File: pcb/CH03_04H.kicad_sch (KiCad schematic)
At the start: 10 parts

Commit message: Corrections to the coax driver
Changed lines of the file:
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@@
     (effects (font (size 1.27 1.27)) (justify right))
   )
-  (symbol (lib_id "Connector:Conn_Coaxial") (at 115.57 59.69 0)
+  (symbol (lib_id "Connector:Conn_Coaxial") (at 115.57 59.69 0) (unit 1)
     (in_bom yes) (on_board yes)
     (property "Reference" "J?" (id 0) (at 118.11 60.325 0)
@@
     (pin "2")
   )
-  (symbol (lib_id "Connector:Conn_Coaxial") (at 115.57 128.27 0)
+  (symbol (lib_id "Connector:Conn_Coaxial") (at 115.57 128.27 0) (unit 1)
     (in_bom yes) (on_board yes)
     (property "Reference" "J?" (id 0) (at 118.11 128.905 0)
@@
     (pin "2")
   )
-  (symbol (lib_id "Device:R") (at 93.98 120.65 270)
+  (symbol (lib_id "Device:R") (at 93.98 120.65 270) (unit 1)
     (in_bom yes) (on_board yes)
     (property "Reference" "R?" (id 0) (at 93.98 115.3922 90))
@@
     (pin "2")
   )
-  (symbol (lib_id "Device:R") (at 115.57 69.85 0)
+  (symbol (lib_id "Device:R") (at 115.57 69.85 0) (unit 1)
     (in_bom yes) (on_board yes)
     (property "Reference" "R?" (id 0) (at 117.348 68.6816 0)
@@
     (pin "2")
   )
-  (symbol (lib_id "power:GND") (at 115.57 87.63 0)
+  (symbol (lib_id "power:GND") (at 115.57 87.63 0) (unit 1)
     (in_bom yes) (on_board yes)
     (property "Reference" "#PWR?" (id 0) (at 115.57 93.98 0)
@@
     (pin "1")
   )
-  (symbol (lib_id "Device:R") (at 115.57 82.55 0)
+  (symbol (lib_id "Device:R") (at 115.57 82.55 0) (unit 1)
     (in_bom yes) (on_board yes)
     (property "Reference" "R?" (id 0) (at 117.348 81.3816 0)
@@
     (pin "2")
   )
-  (symbol (lib_id "Device:R") (at 115.57 138.43 0)
+  (symbol (lib_id "Device:R") (at 115.57 138.43 0) (unit 1)
     (in_bom yes) (on_board yes)
     (property "Reference" "R?" (id 0) (at 117.348 137.2616 0)
@@
     (pin "2")
   )
-  (symbol (lib_id "power:GND") (at 115.57 154.94 0)
+  (symbol (lib_id "power:GND") (at 115.57 154.94 0) (unit 1)
     (in_bom yes) (on_board yes)
     (property "Reference" "#PWR?" (id 0) (at 115.57 161.29 0)
@@
     (pin "1")
   )
-  (symbol (lib_id "Device:R") (at 115.57 149.86 0)
+  (symbol (lib_id "Device:R") (at 115.57 149.86 0) (unit 1)
     (in_bom yes) (on_board yes)
     (property "Reference" "R?" (id 0) (at 117.348 148.6916 0)
@@
     (pin "2")
   )
-  (symbol (lib_id "Device:R") (at 93.98 52.07 270)
+  (symbol (lib_id "Device:R") (at 93.98 52.07 270) (unit 1)
     (in_bom yes) (on_board yes)
     (property "Reference" "R?" (id 0) (at 93.98 46.8122 90))
@@
     (pin "2")
   )
-  (symbol (lib_id "Transistor_BJT:BC856BS") (at 106.68 52.07 0) (mirror x)
+  (symbol (lib_id "Transistor_BJT:BC856BS") (at 106.68 52.07 0) (mirror x) (unit 1)
     (in_bom yes) (on_board yes)
     (property "Reference" "Q?" (id 0) (at 111.506 53.2384 0)
@@
     (pin "6")
   )
-  (symbol (lib_id "Transistor_BJT:BC856BS") (at 106.68 120.65 0) (mirror x)
+  (symbol (lib_id "Transistor_BJT:BC856BS") (at 106.68 120.65 0) (mirror x) (unit 1)
     (in_bom yes) (on_board yes)
     (property "Reference" "Q?" (id 0) (at 111.506 121.8184 0)
@@
       (effects (font (size 1.27 1.27)) hide)
     )
-    (pin "3")
-    (pin "4")
-    (pin "5")
+    (pin "1")
+    (pin "2")
+    (pin "6")
   )
 )

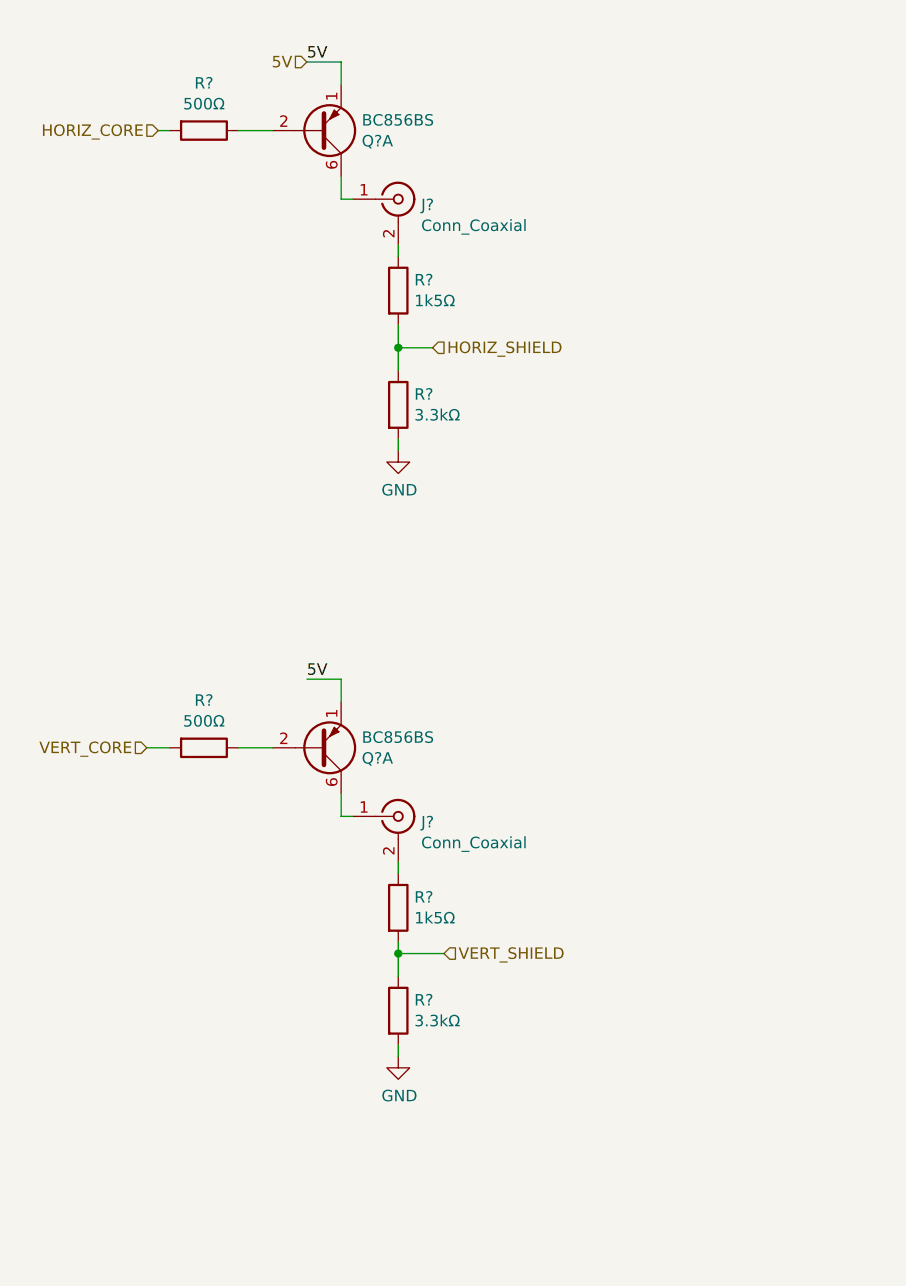
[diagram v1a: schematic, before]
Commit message: Shift register updates - changes the driver from pnp to npn
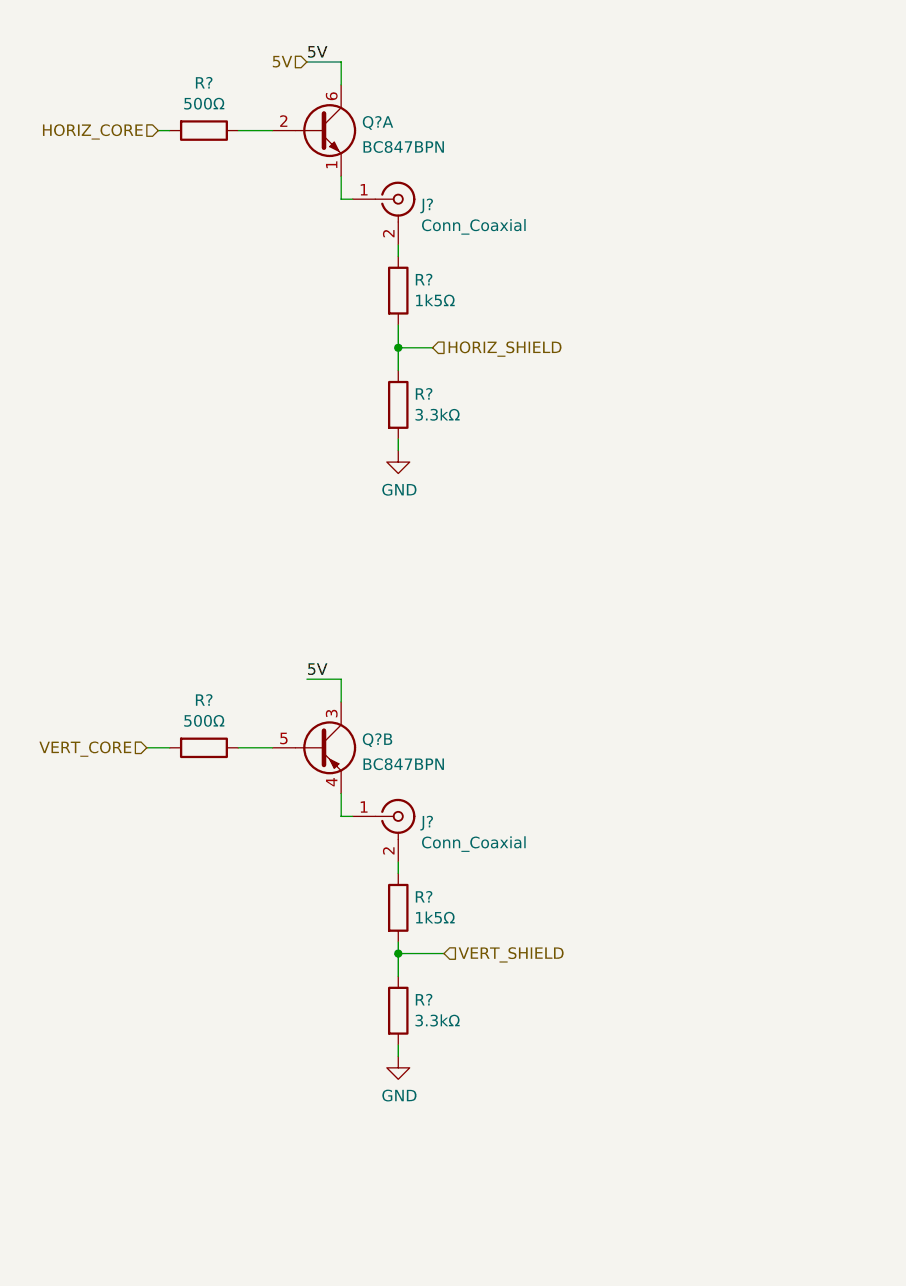
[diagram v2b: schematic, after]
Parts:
- removed Q? (x2): BC856BS, Package_TO_SOT_SMD:SOT-363_SC-70-6, symbol Transistor_BJT:BC856BS
- added Q? (x2): BC847BPN, Package_TO_SOT_SMD:SOT-363_SC-70-6, symbol Transistor_BJT:BC847BPN
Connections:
- net 5V: now also Q?.3 (C2), Q?.6 (C1)
- net at J?.1 (In): now also Q?.1 (E1)
- net at J?.1 (In): now also Q?.4 (E2)
- net at R?.1: now also Q?.5 (B2)
- net at R?.1: now also Q?.2 (B1)
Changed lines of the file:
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@@
     (pin "2")
   )
-  (symbol (lib_id "Transistor_BJT:BC856BS") (at 106.68 52.07 0) (mirror x) (unit 1)
-    (in_bom yes) (on_board yes)
-    (property "Reference" "Q?" (id 0) (at 111.506 53.2384 0)
+  (symbol (lib_id "Transistor_BJT:BC847BPN") (at 106.68 52.07 0) (unit 1)
+    (in_bom yes) (on_board yes) (fields_autoplaced)
+    (property "Reference" "Q?" (id 0) (at 111.5314 51.1615 0)
       (effects (font (size 1.27 1.27)) (justify left))
     )
-    (property "Value" "BC856BS" (id 1) (at 111.506 50.927 0)
+    (property "Value" "BC847BPN" (id 1) (at 111.5314 53.9366 0)
       (effects (font (size 1.27 1.27)) (justify left))
     )
-    (property "Footprint" "Package_TO_SOT_SMD:SOT-363_SC-70-6" (id 2) (at 111.76 54.61 0)
+    (property "Footprint" "Package_TO_SOT_SMD:SOT-363_SC-70-6" (id 2) (at 111.76 49.53 0)
       (effects (font (size 1.27 1.27)) hide)
     )
-    (property "Datasheet" "https://assets.nexperia.com/documents/data-sheet/BC856BS.pdf" (id 3) (at 106.68 52.07 0)
+    (property "Datasheet" "https://assets.nexperia.com/documents/data-sheet/BC847BPN.pdf" (id 3) (at 106.68 52.07 0)
       (effects (font (size 1.27 1.27)) hide)
     )
@@
     (pin "6")
   )
-  (symbol (lib_id "Transistor_BJT:BC856BS") (at 106.68 120.65 0) (mirror x) (unit 1)
-    (in_bom yes) (on_board yes)
-    (property "Reference" "Q?" (id 0) (at 111.506 121.8184 0)
+  (symbol (lib_id "Transistor_BJT:BC847BPN") (at 106.68 120.65 0) (unit 2)
+    (in_bom yes) (on_board yes) (fields_autoplaced)
+    (property "Reference" "Q?" (id 0) (at 111.5314 119.7415 0)
       (effects (font (size 1.27 1.27)) (justify left))
     )
-    (property "Value" "BC856BS" (id 1) (at 111.506 119.507 0)
+    (property "Value" "BC847BPN" (id 1) (at 111.5314 122.5166 0)
       (effects (font (size 1.27 1.27)) (justify left))
     )
-    (property "Footprint" "Package_TO_SOT_SMD:SOT-363_SC-70-6" (id 2) (at 111.76 123.19 0)
+    (property "Footprint" "Package_TO_SOT_SMD:SOT-363_SC-70-6" (id 2) (at 111.76 118.11 0)
       (effects (font (size 1.27 1.27)) hide)
     )
-    (property "Datasheet" "https://assets.nexperia.com/documents/data-sheet/BC856BS.pdf" (id 3) (at 106.68 120.65 0)
+    (property "Datasheet" "https://assets.nexperia.com/documents/data-sheet/BC847BPN.pdf" (id 3) (at 106.68 120.65 0)
       (effects (font (size 1.27 1.27)) hide)
     )
-    (pin "1")
-    (pin "2")
-    (pin "6")
+    (pin "3")
+    (pin "4")
+    (pin "5")
   )
 )

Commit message: Adds line protection
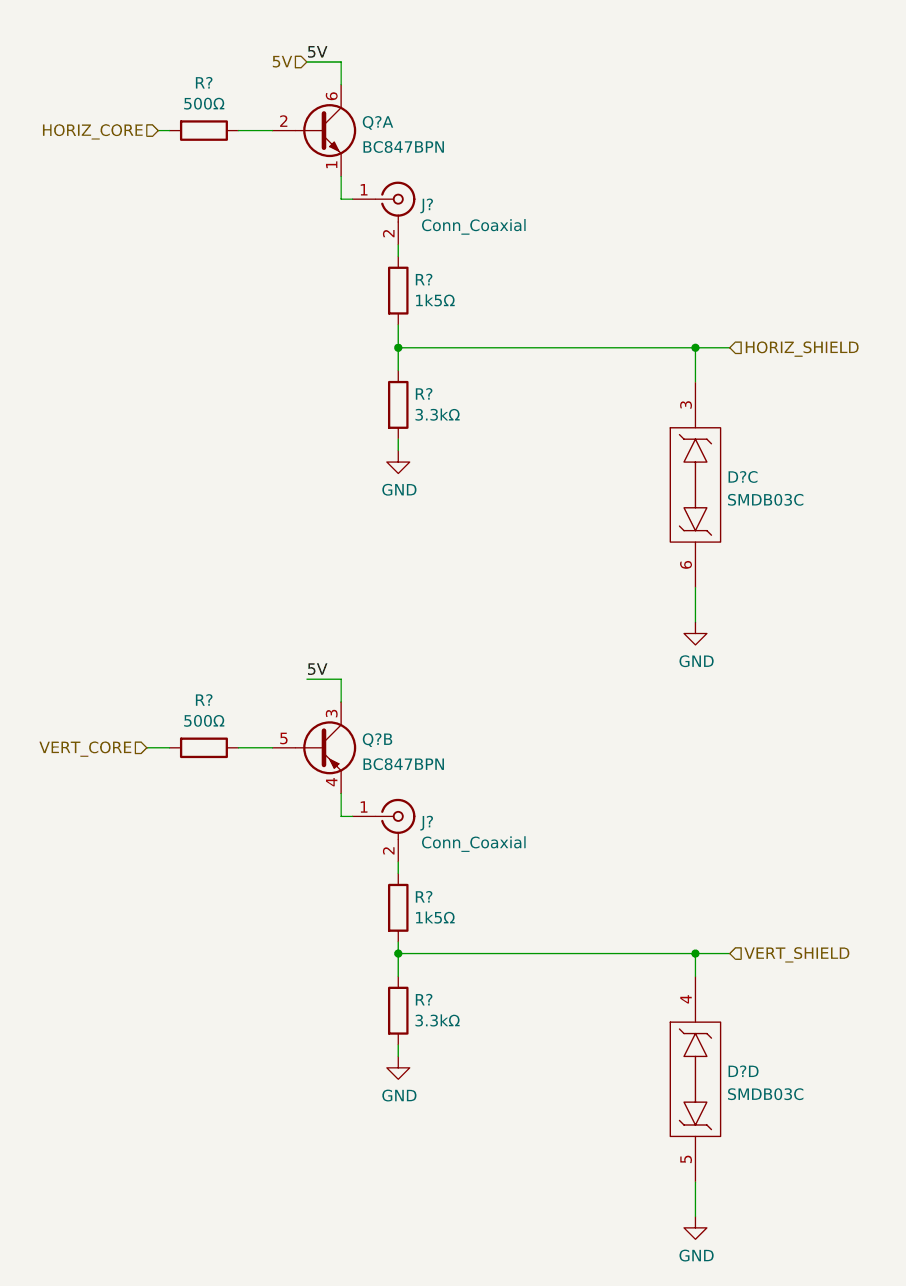
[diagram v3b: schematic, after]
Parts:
- added D? (x2): SMDB03C, Package_SO:SO-8_3.9x4.9mm_P1.27mm, symbol CoaxTester:SMDB03C
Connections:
- net GND: now also D?.5, D?.6
- net HORIZ_SHIELD: now also D?.3
- net VERT_SHIELD: now also D?.4
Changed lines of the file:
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@@
   (junction (at 115.57 76.2) (diameter 0) (color 0 0 0 0)
   )
+  (junction (at 148.59 76.2) (diameter 0) (color 0 0 0 0)
+  )
+  (junction (at 148.59 143.51) (diameter 0) (color 0 0 0 0)
+  )
   (junction (at 115.57 143.51) (diameter 0) (color 0 0 0 0)
   )
@@
     (stroke (width 0) (type default) (color 0 0 0 0))
   )
-  (wire (pts (xy 115.57 143.51) (xy 120.65 143.51))
+  (wire (pts (xy 115.57 143.51) (xy 148.59 143.51))
     (stroke (width 0) (type default) (color 0 0 0 0))
   )
@@
     (stroke (width 0) (type default) (color 0 0 0 0))
   )
-  (wire (pts (xy 115.57 76.2) (xy 119.38 76.2))
+  (wire (pts (xy 115.57 76.2) (xy 148.59 76.2))
     (stroke (width 0) (type default) (color 0 0 0 0))
   )
@@
     (stroke (width 0) (type default) (color 0 0 0 0))
   )
+  (wire (pts (xy 148.59 76.2) (xy 148.59 80.01))
+    (stroke (width 0) (type default) (color 0 0 0 0))
+  )
   (wire (pts (xy 115.57 133.35) (xy 115.57 134.62))
     (stroke (width 0) (type default) (color 0 0 0 0))
@@
     (stroke (width 0) (type default) (color 0 0 0 0))
   )
+  (wire (pts (xy 148.59 168.91) (xy 148.59 172.72))
+    (stroke (width 0) (type default) (color 0 0 0 0))
+  )
   (wire (pts (xy 97.79 52.07) (xy 101.6 52.07))
     (stroke (width 0) (type default) (color 0 0 0 0))
@@
     (stroke (width 0) (type default) (color 0 0 0 0))
   )
+  (wire (pts (xy 148.59 143.51) (xy 152.4 143.51))
+    (stroke (width 0) (type default) (color 0 0 0 0))
+  )
   (wire (pts (xy 115.57 143.51) (xy 115.57 146.05))
     (stroke (width 0) (type default) (color 0 0 0 0))
   )
+  (wire (pts (xy 148.59 143.51) (xy 148.59 146.05))
+    (stroke (width 0) (type default) (color 0 0 0 0))
+  )
+  (wire (pts (xy 148.59 76.2) (xy 152.4 76.2))
+    (stroke (width 0) (type default) (color 0 0 0 0))
+  )
   (wire (pts (xy 115.57 86.36) (xy 115.57 87.63))
     (stroke (width 0) (type default) (color 0 0 0 0))
   )
   (wire (pts (xy 109.22 125.73) (xy 109.22 128.27))
+    (stroke (width 0) (type default) (color 0 0 0 0))
+  )
+  (wire (pts (xy 148.59 102.87) (xy 148.59 106.68))
     (stroke (width 0) (type default) (color 0 0 0 0))
   )
@@
     (effects (font (size 1.27 1.27)) (justify right))
   )
-  (hierarchical_label "VERT_SHIELD" (shape input) (at 120.65 143.51 0)
+  (hierarchical_label "VERT_SHIELD" (shape input) (at 152.4 143.51 0)
     (effects (font (size 1.27 1.27)) (justify left))
   )
-  (hierarchical_label "HORIZ_SHIELD" (shape input) (at 119.38 76.2 0)
+  (hierarchical_label "HORIZ_SHIELD" (shape input) (at 152.4 76.2 0)
     (effects (font (size 1.27 1.27)) (justify left))
   )
@@
     (pin "6")
   )
+  (symbol (lib_id "CoaxTester:SMDB03C") (at 148.59 157.48 0) (unit 4)
+    (in_bom yes) (on_board yes) (fields_autoplaced)
+    (property "Reference" "D?" (id 0) (at 152.0952 156.6453 0)
+      (effects (font (size 1.27 1.27)) (justify left))
+    )
+    (property "Value" "SMDB03C" (id 1) (at 152.0952 159.1822 0)
+      (effects (font (size 1.27 1.27)) (justify left))
+    )
+    (property "Footprint" "Package_SO:SO-8_3.9x4.9mm_P1.27mm" (id 2) (at 148.59 156.21 0)
+      (effects (font (size 1.27 1.27)) hide)
+    )
+    (property "Datasheet" "https://www.smc-diodes.com/propdf/SMDB03C%20THRU%20SMDB24C%20N0426%20REV.A.pdf" (id 3) (at 148.59 156.21 0)
+      (effects (font (size 1.27 1.27)) hide)
+    )
+    (pin "4")
+    (pin "5")
+  )
   (symbol (lib_id "Transistor_BJT:BC847BPN") (at 106.68 120.65 0) (unit 2)
     (in_bom yes) (on_board yes) (fields_autoplaced)
@@
     (pin "5")
   )
+  (symbol (lib_id "CoaxTester:SMDB03C") (at 148.59 91.44 0) (unit 3)
+    (in_bom yes) (on_board yes) (fields_autoplaced)
+    (property "Reference" "D?" (id 0) (at 152.0952 90.6053 0)
+      (effects (font (size 1.27 1.27)) (justify left))
+    )
+    (property "Value" "SMDB03C" (id 1) (at 152.0952 93.1422 0)
+      (effects (font (size 1.27 1.27)) (justify left))
+    )
+    (property "Footprint" "Package_SO:SO-8_3.9x4.9mm_P1.27mm" (id 2) (at 148.59 90.17 0)
+      (effects (font (size 1.27 1.27)) hide)
+    )
+    (property "Datasheet" "https://www.smc-diodes.com/propdf/SMDB03C%20THRU%20SMDB24C%20N0426%20REV.A.pdf" (id 3) (at 148.59 90.17 0)
+      (effects (font (size 1.27 1.27)) hide)
+    )
+    (pin "3")
+    (pin "6")
+  )
+  (symbol (lib_id "power:GND") (at 148.59 106.68 0) (unit 1)
+    (in_bom yes) (on_board yes)
+    (property "Reference" "#PWR?" (id 0) (at 148.59 113.03 0)
+      (effects (font (size 1.27 1.27)) hide)
+    )
+    (property "Value" "GND" (id 1) (at 148.717 111.0742 0))
+    (property "Footprint" "" (id 2) (at 148.59 106.68 0)
+      (effects (font (size 1.27 1.27)) hide)
+    )
+    (property "Datasheet" "" (id 3) (at 148.59 106.68 0)
+      (effects (font (size 1.27 1.27)) hide)
+    )
+    (pin "1")
+  )
+  (symbol (lib_id "power:GND") (at 148.59 172.72 0) (unit 1)
+    (in_bom yes) (on_board yes)
+    (property "Reference" "#PWR?" (id 0) (at 148.59 179.07 0)
+      (effects (font (size 1.27 1.27)) hide)
+    )
+    (property "Value" "GND" (id 1) (at 148.717 177.1142 0))
+    (property "Footprint" "" (id 2) (at 148.59 172.72 0)
+      (effects (font (size 1.27 1.27)) hide)
+    )
+    (property "Datasheet" "" (id 3) (at 148.59 172.72 0)
+      (effects (font (size 1.27 1.27)) hide)
+    )
+    (pin "1")
+  )
 )

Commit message: Schematic complete
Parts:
- gave numbers to parts that had none: 10
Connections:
- net 5V renamed +5V

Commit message: DRC OK
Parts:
- renumbered D301 to D201
